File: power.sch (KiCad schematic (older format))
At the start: 58 parts, among them Q2 2N7002, Q3 2N7002, SW1 Pushbutton, U10 LT1965, U11 INA213-SC70, U12 MCP73831, U13 DRV8839, U14 DRV8839, U8 LTC2955DDB-1, U9 LT1965

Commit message: Regenerate netlist & Start placing footprints
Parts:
- D10, D11, D12, D13, D14, D15, D16, D8, D9: footprint LEDs:LED-0603 -> _std:_LED_0603
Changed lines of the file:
@@
 EESchema Schematic File Version 2
-LIBS:speedy-rescue
 LIBS:speedy-cache
 LIBS:power
@@
 F 0 "D8" H 4650 3725 50  0000 C CNN
 F 1 "CHARGE_LED" H 4650 3525 39  0000 C CNN
-F 2 "LEDs:LED-0603" H 4650 3625 60  0001 C CNN
+F 2 "_std:_LED_0603" H 4650 3625 60  0001 C CNN
 F 3 "" H 4650 3625 60  0000 C CNN
 	1    4650 3625
@@
 F 0 "D9" V 8250 4650 50  0000 C CNN
 F 1 "APT1608F3C" V 8150 4725 39  0000 C CNN
-F 2 "LEDs:LED-0603" H 8250 4525 60  0001 C CNN
+F 2 "_std:_LED_0603" H 8250 4525 60  0001 C CNN
 F 3 "" H 8250 4525 60  0000 C CNN
 	1    8250 4525
@@
 F 0 "D10" V 8250 5100 50  0000 C CNN
 F 1 "APT1608F3C" V 8150 5175 39  0000 C CNN
-F 2 "LEDs:LED-0603" H 8250 4975 60  0001 C CNN
+F 2 "_std:_LED_0603" H 8250 4975 60  0001 C CNN
 F 3 "" H 8250 4975 60  0000 C CNN
 	1    8250 4975
@@
 F 0 "D12" V 8750 5100 50  0000 C CNN
 F 1 "APT1608F3C" V 8650 5175 39  0000 C CNN
-F 2 "LEDs:LED-0603" H 8750 4975 60  0001 C CNN
+F 2 "_std:_LED_0603" H 8750 4975 60  0001 C CNN
 F 3 "" H 8750 4975 60  0000 C CNN
 	1    8750 4975
@@
 F 0 "D11" V 8750 4650 50  0000 C CNN
 F 1 "APT1608F3C" V 8650 4725 39  0000 C CNN
-F 2 "LEDs:LED-0603" H 8750 4525 60  0001 C CNN
+F 2 "_std:_LED_0603" H 8750 4525 60  0001 C CNN
 F 3 "" H 8750 4525 60  0000 C CNN
 	1    8750 4525
@@
 F 0 "D13" V 9975 4675 50  0000 C CNN
 F 1 "APT1608F3C" V 9875 4750 39  0000 C CNN
-F 2 "LEDs:LED-0603" H 9975 4550 60  0001 C CNN
+F 2 "_std:_LED_0603" H 9975 4550 60  0001 C CNN
 F 3 "" H 9975 4550 60  0000 C CNN
 	1    9975 4550
@@
 F 0 "D14" V 9975 5125 50  0000 C CNN
 F 1 "APT1608F3C" V 9875 5200 39  0000 C CNN
-F 2 "LEDs:LED-0603" H 9975 5000 60  0001 C CNN
+F 2 "_std:_LED_0603" H 9975 5000 60  0001 C CNN
 F 3 "" H 9975 5000 60  0000 C CNN
 	1    9975 5000
@@
 F 0 "D16" V 10475 5125 50  0000 C CNN
 F 1 "APT1608F3C" V 10375 5200 39  0000 C CNN
-F 2 "LEDs:LED-0603" H 10475 5000 60  0001 C CNN
+F 2 "_std:_LED_0603" H 10475 5000 60  0001 C CNN
 F 3 "" H 10475 5000 60  0000 C CNN
 	1    10475 5000
@@
 F 0 "D15" V 10475 4675 50  0000 C CNN
 F 1 "APT1608F3C" V 10375 4750 39  0000 C CNN
-F 2 "LEDs:LED-0603" H 10475 4550 60  0001 C CNN
+F 2 "_std:_LED_0603" H 10475 4550 60  0001 C CNN
 F 3 "" H 10475 4550 60  0000 C CNN
 	1    10475 4550

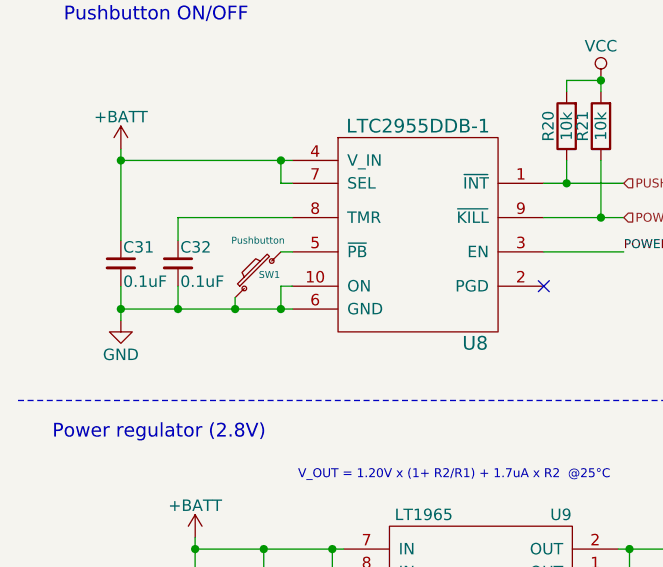
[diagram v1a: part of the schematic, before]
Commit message: Change pushbutton for a radially mounted button
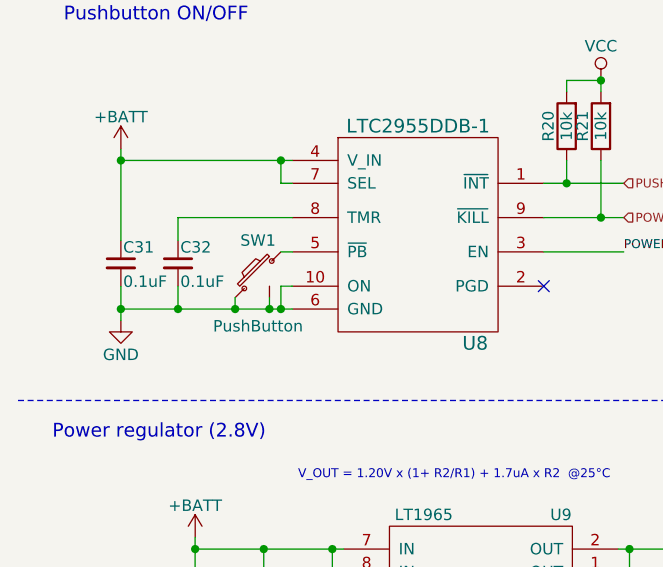
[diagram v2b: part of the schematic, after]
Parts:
- removed SW1: Pushbutton, _div:_PTS525SK15-SMT-Pushbutton, symbol SW_PUSH_SMALL
- added SW1: PushButton, _div:SMD_Pushbutton_B3U-3100P, symbol PushButton_B3U
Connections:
- net GND: now also SW1.2, SW1.3 (GND)
- net at U8.5 (~PB): now also SW1.1
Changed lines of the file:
@@
-$EndComp
-$Comp
-L SW_PUSH_SMALL SW1
-U 1 1 554459C4
-P 1525 3900
-F 0 "SW1" V 1525 3850 30  0000 C CNN
-F 1 "Pushbutton" V 1675 3900 30  0000 C CNN
-F 2 "_div:_PTS525SK15-SMT-Pushbutton" H 1525 3900 60  0001 C CNN
-F 3 "" H 1525 3900 60  0000 C CNN
-	1    1525 3900
-	0    -1   -1   0
 $EndComp
 $Comp
@@
 Text HLabel 1850 7275 0    39   Input ~ 0
 SENSOR_EN
+$Comp
+L PushButton_B3U SW1
+U 1 1 56AA1F82
+P 1525 3900
+F 0 "SW1" H 1525 4050 50  0000 C CNN
+F 1 "PushButton" H 1525 3675 50  0000 C CNN
+F 2 "_div:SMD_Pushbutton_B3U-3100P" H 1525 3900 50  0001 C CNN
+F 3 "" H 1525 3900 50  0000 C CNN
+	1    1525 3900
+	-1   0    0    -1
+$EndComp
+Wire Wire Line
+	1575 4000 1575 4050
+Connection ~ 1575 4050
 $EndSCHEMATC

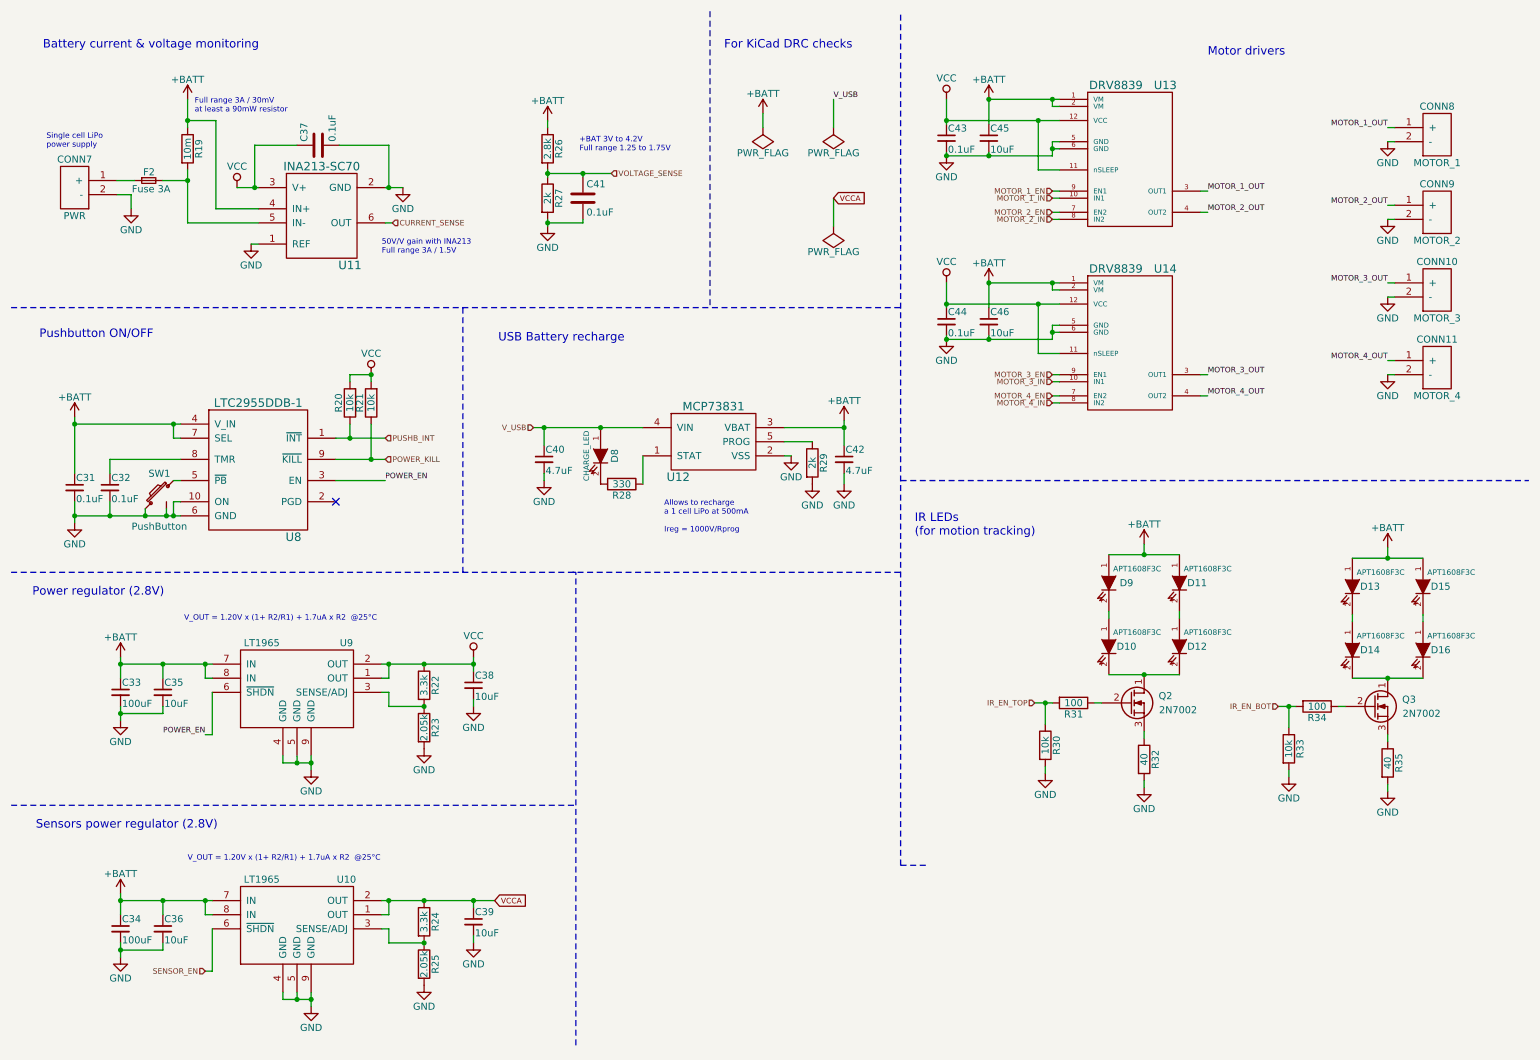
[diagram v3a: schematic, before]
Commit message: Fix problems noted by @nuft during review
- Force pulldown on unused bootloadr pins (USART 1 & 3)
- Use one oscillator for both MCU and NRF
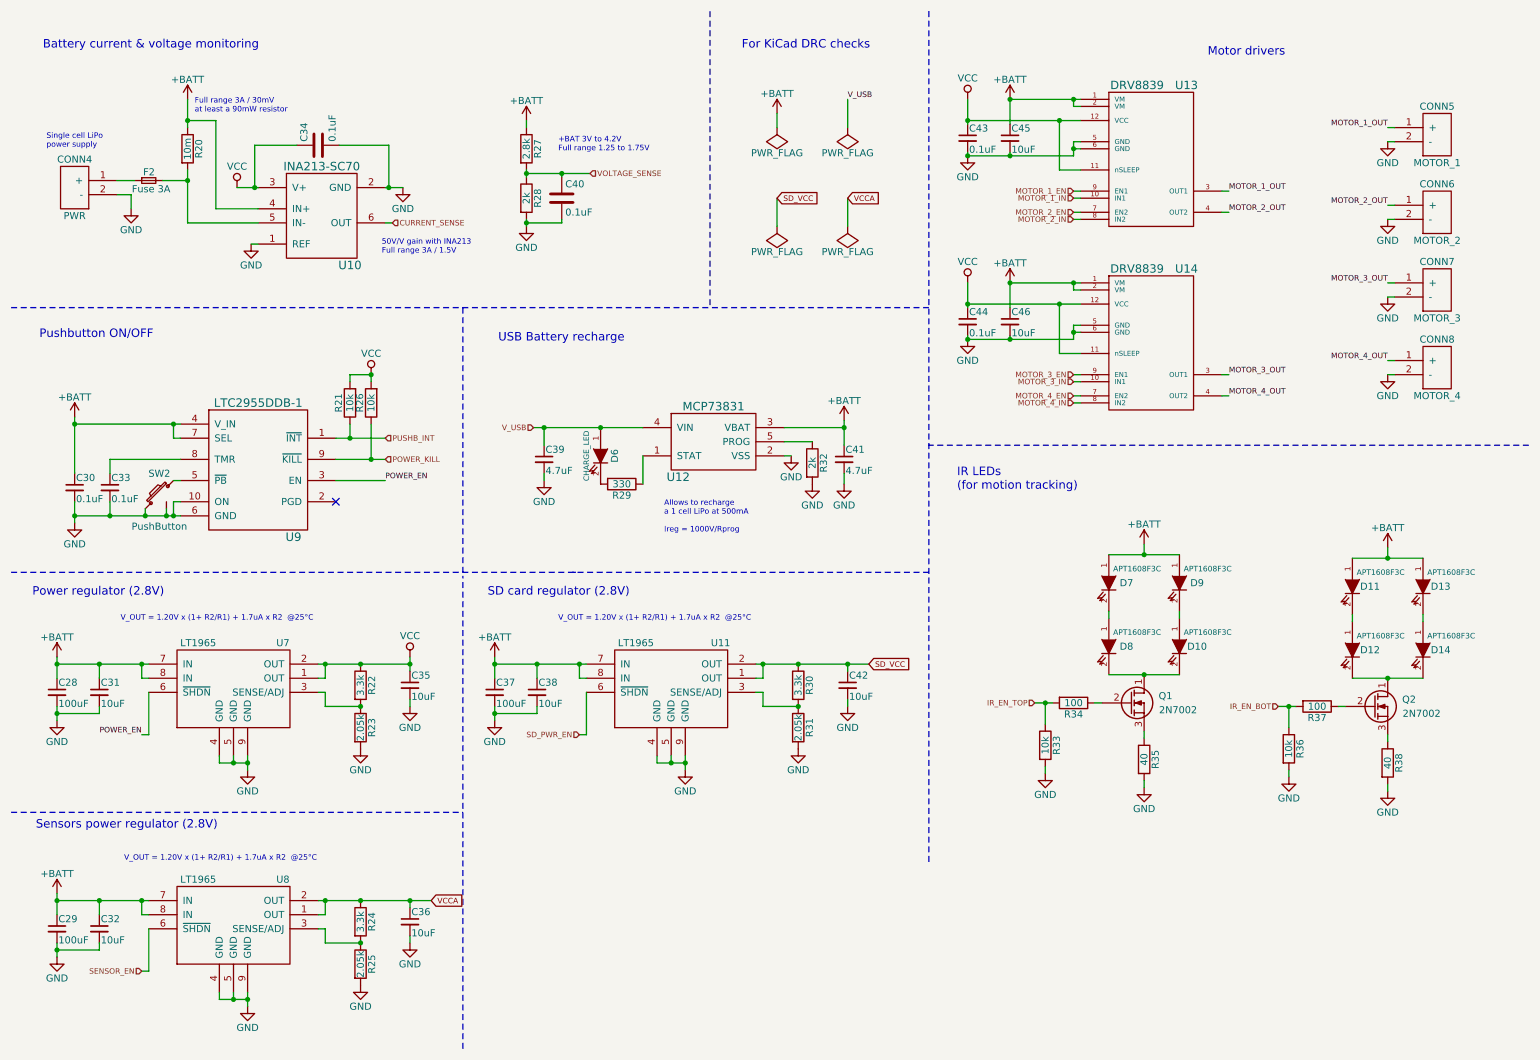
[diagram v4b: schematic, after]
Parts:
- added C37: 100uF, _std:_0402, symbol C_Small
- added C38, C42: 10uF, _std:_0603, symbol C_Small
- added R30: 3.3k, _std:_0402, symbol R
- added R31: 2.05k, _std:_0402, symbol R
- added U11: LT1965, Housings_DFN_QFN:DFN-8-1EP_3x3mm_Pitch0.5mm, symbol LT1965
- renumbered C33 to C28, C34 to C29, C31 to C30, C35 to C31, C36 to C32, C32 to C33, C37 to C34, C38 to C35, C39 to C36, C40 to C39, C41 to C40, C42 to C41, CONN7 to CONN4, CONN8 to CONN5, CONN9 to CONN6, CONN10 to CONN7, CONN11 to CONN8, D12 to D10, D13 to D11, D14 to D12, D15 to D13, D16 to D14, D8 to D6, D9 to D7, D10 to D8, D11 to D9, Q2 to Q1, Q3 to Q2, R19 to R20, R20 to R21, R21 to R26, R26 to R27, R27 to R28, R28 to R29, R29 to R32, R30 to R33, R31 to R34, R32 to R35, R33 to R36, R34 to R37, R35 to R38, SW1 to SW2, U11 to U10, U9 to U7, U10 to U8, U8 to U9
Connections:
- net +BATT: now also C37.1, C38.1, U11.7 (IN), U11.8 (IN)
- net GND: now also C37.2, C38.2, C42.2, R31.2, U11.4 (GND), U11.5 (GND), U11.9 (GND)
- new net: R30.2, R31.1, U11.3 (SENSE/ADJ)
- new net SD_PWR_EN: U11.6 (~SHDN)
- new net SD_VCC: C42.1, R30.1, U11.1 (OUT), U11.2 (OUT)
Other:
- note added: "SD card regulator (2.8V)\n"
- moved on the sheet: C28, C29, C31, C32, C35, C36, C40, C43, C44, C45, C46, R22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

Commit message: (Re)Place components on PCB
Netlist was broken after review corrections
Rebuilt and placed components from scratch
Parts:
- C28, C29, C37: footprint _std:_0402 -> _std:_0603
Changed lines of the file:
@@
 F 0 "C28" H 810 5370 50  0000 L CNN
 F 1 "100uF" H 810 5220 50  0000 L CNN
-F 2 "_std:_0402" H 800 5300 60  0001 C CNN
+F 2 "_std:_0603" H 800 5300 60  0001 C CNN
 F 3 "" H 800 5300 60  0000 C CNN
 	1    800  5300
@@
 F 0 "C29" H 810 7045 50  0000 L CNN
 F 1 "100uF" H 810 6895 50  0000 L CNN
-F 2 "_std:_0402" H 800 6975 60  0001 C CNN
+F 2 "_std:_0603" H 800 6975 60  0001 C CNN
 F 3 "" H 800 6975 60  0000 C CNN
 	1    800  6975
@@
 F 0 "C37" H 3910 5370 50  0000 L CNN
 F 1 "100uF" H 3910 5220 50  0000 L CNN
-F 2 "_std:_0402" H 3900 5300 60  0001 C CNN
+F 2 "_std:_0603" H 3900 5300 60  0001 C CNN
 F 3 "" H 3900 5300 60  0000 C CNN
 	1    3900 5300
